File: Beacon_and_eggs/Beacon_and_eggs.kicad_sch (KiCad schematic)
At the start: 71 parts, among them J1 USB_C_Receptacle_USB2.0_16P, J2 Conn_01x03_Pin, J3 Conn_01x02_Pin, Q1 NTA4151P, Q2 NTA4153N, SW3 RESET, SW4 BOOT0, U1 SA868S, U2 STM32F411CEU6TR, U3 ADXL343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

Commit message: reduce drc error to 0, updated step file
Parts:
- C1, C10, C11, C12, C13, C14, C15, C16, C17, C18, C20, C21, C22, C23, C24, C25, C7, C8, C9: footprint Capacitor_SMD:C_0402_1005Metric_Pad0.74x0.62mm_HandSolder -> Capacitor_SMD:C_0402_1005Metric
- C19: footprint Capacitor_SMD:C_0805_2012Metric -> Capacitor_SMD:C_0402_1005Metric
- C2, C3, C4, C5, C6: footprint Capacitor_SMD:C_0201_0603Metric_Pad0.64x0.40mm_HandSolder -> Capacitor_SMD:C_0201_0603Metric
- D1, D3: footprint Diode_SMD:D_0402_1005Metric_Pad0.77x0.64mm_HandSolder -> Diode_SMD:D_0402_1005Metric
- D2, D5: footprint LED_SMD:LED_0402_1005Metric_Pad0.77x0.64mm_HandSolder -> LED_SMD:LED_0402_1005Metric
- R1, R10, R11, R12, R13, R14, R15, R16, R17, R18, R19, R2, R20, R21, R3, R4, R5, R6, R7, R8, R9: footprint Resistor_SMD:R_0402_1005Metric_Pad0.72x0.64mm_HandSolder -> Resistor_SMD:R_0402_1005Metric
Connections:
- net GND: now also U6.21 (EPAD)
- no-connect marks 30 -> 29

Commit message: changed batery connector footprint from vert. to horz.
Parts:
- removed C11: 0.1uF, Capacitor_SMD:C_0402_1005Metric, symbol Device:C
- removed J3: Conn_01x02_Pin, Connector_JST:JST_PH_B2B-PH-K_1x02_P2.00mm_Vertical, symbol Connector:Conn_01x02_Pin
- removed R1, R2: 10k, Resistor_SMD:R_0402_1005Metric, symbol Device:R
- removed SW4: BOOT0, Button_Switch_SMD:SW_SPST_PTS810, symbol Switch:SW_MEC_5G
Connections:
- net BOOT0: no longer names the net of U2.44 (BOOT0)
- no-connect marks 29 -> 30
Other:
- note removed: "BOOT CIRCUIT"

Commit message: updated step file, added 3D components
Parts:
- added C26: 0.1uF, Capacitor_SMD:C_0402_1005Metric, symbol Device:C
- added J3: Conn_01x02_Pin, Connector_JST:JST_XH_S2B-XH-A_1x02_P2.50mm_Horizontal, symbol Connector:Conn_01x02_Pin
- added R22: 10k, Resistor_SMD:R_0402_1005Metric, symbol Device:R
- added R25: 10K, Resistor_SMD:R_0402_1005Metric, symbol Device:R
- added SW4: BOOT0, Button_Switch_SMD:SW_SPST_PTS810, symbol Switch:SW_MEC_5G
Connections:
- net +3.3V: now also SW4.3 (B), SW4.4 (B)
- net BOOT1: now also R25.2
- net GND: now also C26.2, J3.2 (Pin_2), R22.1, R25.1
- net VBAT: now also J3.1 (Pin_1)
- net BOOT0: now reaches U2.44 (BOOT0)
- net BOOT0: now also C26.1, R22.2, SW4.1 (A), SW4.2 (A)
- no-connect marks 30 -> 29
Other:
- note added: "BOOT CIRCUIT"
- note added: "With the ALT ADDRESS pin high, the 7-bit I2C address for the device is 0x1D, followed by the R/W bit. This translates to 0x3A for a write and 0x3B for a read"

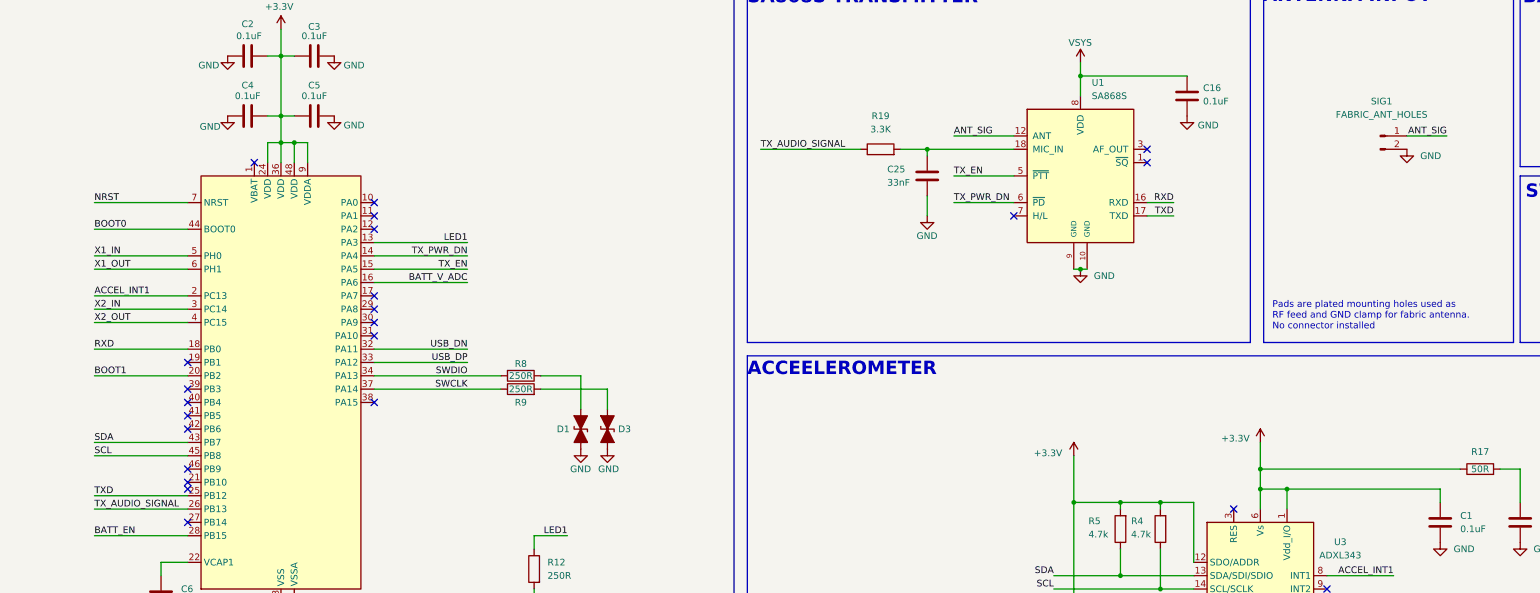
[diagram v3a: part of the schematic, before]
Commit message: changed UART software  pins to hardware pins, fixed I2C pins
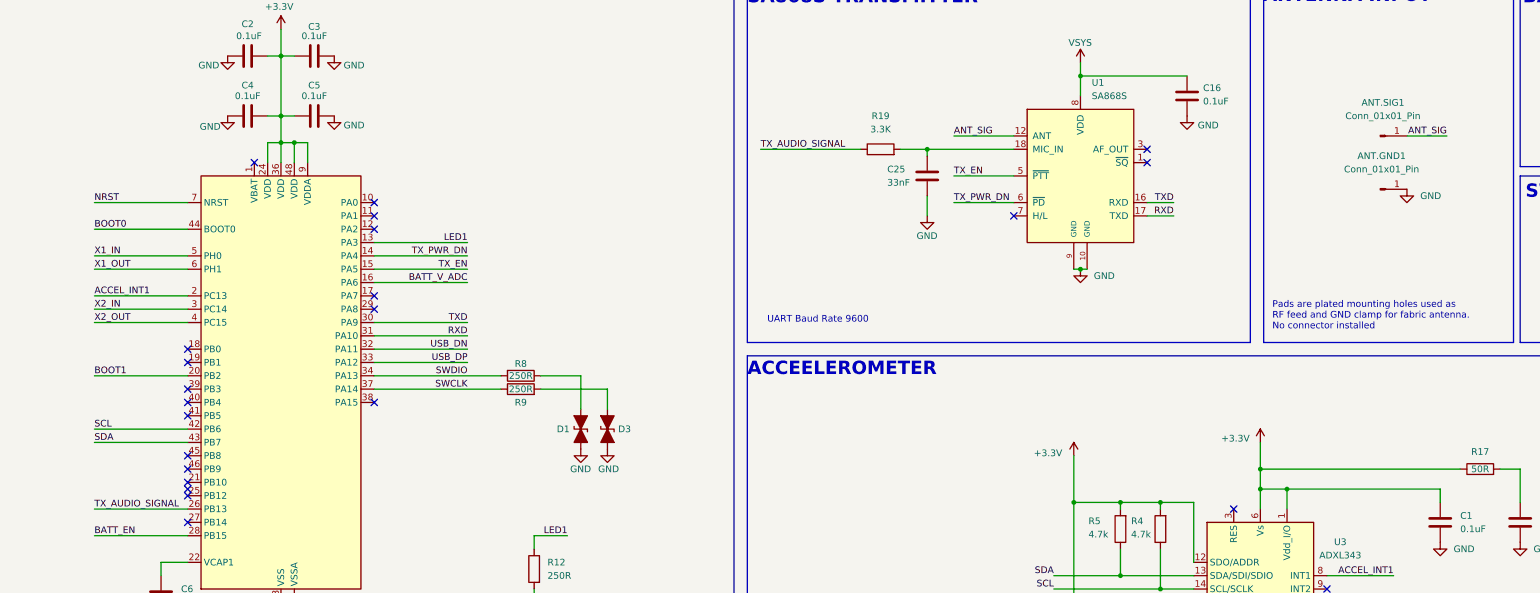
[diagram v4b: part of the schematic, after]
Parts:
- removed SIG1: FABRIC_ANT_HOLES, MountingHole:MountingHole_3.2mm_M3_DIN965_Pad_TopBottom, symbol Connector:Conn_01x02_Pin
- added ANT.GND1, ANT.SIG1: Conn_01x01_Pin, MountingHole:MountingHole_3.2mm_M3_DIN965_Pad_TopBottom, symbol Connector:Conn_01x01_Pin
- R25: DigiKey_Part_Number (none) -> RMCF0402FT10K0
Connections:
- net ANT_SIG: now also ANT.SIG1.1 (Pin_1)
- net GND: now also ANT.GND1.1 (Pin_1)
- net RXD: now also U1.17 (TXD), U2.31 (PA10); no longer U1.16 (RXD), U2.18 (PB0)
- net SCL: now also U2.42 (PB6); no longer U2.45 (PB8)
- net TXD: now also U1.16 (RXD), U2.30 (PA9); no longer U1.17 (TXD), U2.25 (PB12)
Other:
- note added: "UART Baud Rate 9600"

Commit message: labelled switches
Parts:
- ANT.GND1, ANT.SIG1, J3: now left out of the parts list
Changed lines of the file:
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@@
 		(body_style 1)
 		(exclude_from_sim no)
-		(in_bom yes)
+		(in_bom no)
 		(on_board yes)
 		(in_pos_files yes)
@@
 		(body_style 1)
 		(exclude_from_sim no)
-		(in_bom yes)
+		(in_bom no)
 		(on_board yes)
 		(in_pos_files yes)
@@
 		(body_style 1)
 		(exclude_from_sim no)
-		(in_bom yes)
+		(in_bom no)
 		(on_board yes)
 		(in_pos_files yes)

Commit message: Updated two digipart numbers and remade BOM
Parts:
- C19: DigiKey_Part_Number C2012X5R0J336M125AC -> GRM155R60J156ME15D
- C6: DigiKey_Part_Number GRM155R60J475ME87D -> GRM035R60J475ME15J
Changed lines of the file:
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@@
 			)
 		)
-		(property "DigiKey_Part_Number" "GRM155R60J475ME87D"
+		(property "DigiKey_Part_Number" "GRM035R60J475ME15J"
 			(at 105.41 208.2799 0)
 			(hide yes)
@@
 			)
 		)
-		(property "DigiKey_Part_Number" "C2012X5R0J336M125AC"
+		(property "DigiKey_Part_Number" "GRM155R60J156ME15D"
 			(at 120.65 62.2299 0)
 			(hide yes)
@@
 			)
 		)
+		(property "Untitled Field" ""
+			(at 116.84 59.69 0)
+			(hide yes)
+			(show_name no)
+			(do_not_autoplace no)
+			(effects
+				(font
+					(size 1.27 1.27)
+				)
+			)
+		)
